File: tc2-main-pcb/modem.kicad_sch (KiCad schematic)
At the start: 15 parts, among them J7 Screw_Terminal_01x01, J8 Conn_01x03, U12 SIM7600G-H-M.2

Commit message: P2 milestone
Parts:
- removed C37: 220nF, Capacitor_SMD:C_0402_1005Metric, symbol Device:C_Small
- removed Card1: SIM-Nano, cacophony-library:SIM-SMD_SMN-304, symbol cacophony-library:SIM-Nano
- removed D4: SMF05CT1G, cacophony-library:SOT-363_L2.0-W1.3-P0.65-LS2.1-BR, symbol cacophony-library:SMF05CT1G
- removed J8: Conn_01x03, Connector_PinHeader_2.54mm:PinHeader_1x03_P2.54mm_Vertical, symbol Connector_Generic:Conn_01x03
- added J11: Conn_01x08, cacophony-library:sim-usb-pcb, symbol Connector_Generic:Conn_01x08
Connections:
- net 4G_USB_D+: now also J11.7 (Pin_7)
- net 4G_USB_D-: now also J11.8 (Pin_8)
- net GND: now also J11.3 (Pin_3), J11.6 (Pin_6)
- net USIM_CLK: now reaches R26.2
- net USIM_CLK: now also J11.2 (Pin_2)
- net USIM_VDD: now reaches U12.36 (USIM_VDD)
- net USIM_VDD: now also J11.5 (Pin_5)
- net USIM_RST: now reaches R25.2
- net USIM_RST: now also J11.1 (Pin_1)
- net USIM_DATA: now reaches R27.2
- net USIM_DATA: now also J11.4 (Pin_4)
- no-connect marks 48 -> 46
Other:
- moved on the sheet: R25, R26, R27

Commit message: P3-Nov release
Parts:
- removed C32, C36: 10uF, Capacitor_SMD:C_0603_1608Metric, symbol Device:C_Small
- added C1 (x4): 220nF, Capacitor_SMD:C_0402_1005Metric, symbol Device:C_Small
- added C4 (x3): 12pF, Capacitor_SMD:C_0402_1005Metric, symbol Device:C_Small
- added C49, C52, C53, C54, C55, C57, C58, C59, C60: 22uF, Capacitor_SMD:C_0603_1608Metric, symbol Device:C_Small
- added FB1: FerriteBead, Inductor_SMD:L_0805_2012Metric, symbol Device:FerriteBead
- added L3: INDUCTOR, Inductor_SMD:L_1008_2520Metric, symbol cacophony-library:Power_Inductor
- added R42, R43: 1M, Resistor_SMD:R_0402_1005Metric, symbol Device:R
- added R44: 100k, Resistor_SMD:R_0402_1005Metric, symbol Device:R
- added R45: 150k, Resistor_SMD:R_0402_1005Metric, symbol Device:R
- added TP3: TP_2P, cacophony-library:test-point-2p, symbol cacophony-library:TestPoint_2Pole
- added U5: TPS6302x, cacophony-library:VSON-14_L4.0-W3.0-P0.50-BL-EP_TI_DSJ, symbol cacophony-library:TPS6302x
- C33, C34, C35: value 10uF -> 22uF; LCSC C19702 -> C2980159
- J7: footprint cacophony-library:SMD_BD4.4-L4.4-D2.8 -> cacophony-library:M2_modem_mount_screw; LCSC C2928178 -> C2928176
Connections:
- net +3V3: no longer C33.1, C34.1, C35.1, U12.2 (VBAT), U12.4 (VBAT), U12.70 (VBAT), U12.72 (VBAT), U12.74 (VBAT)
- net GND: now also C1.1, C1.1, C1.1, C1.1, C4.1, C4.1, C4.1, C49.2, C52.2, C53.2, C54.2, C55.2, C57.2, C58.2, C59.2, C60.2, R44.2, R45.2, TP3.1, U5.15 (PGND), U5.2 (GND)
- new net: R43.2, U5.14 (PG)
- new net: R42.2, R45.1, U5.3 (FB)
- new net +3V8: C1.2, C1.2, C33.1, C34.1, C35.1, C4.2, C4.2, C57.1, C58.1, C59.1, FB1.2, TP3.2, U12.2 (VBAT), U12.4 (VBAT), U12.70 (VBAT), U12.72 (VBAT), U12.74 (VBAT)
- new net +5V: C1.2, C4.2, C54.1, C55.1, U5.10 (VIN), U5.11 (VIN)
- new net 3V3_L1: L3.1, U5.8 (L1), U5.9 (L1)
- new net 3V3_L2: L3.2, U5.6 (L2), U5.7 (L2)
- new net MODEM_3V8: C1.2, C49.1, C52.1, C53.1, C60.1, FB1.1, R42.1, R43.1, U5.4 (VOUT), U5.5 (VOUT)
- new net MODEM_POWER_EN: R44.1, U5.12 (EN)
- no-connect marks 46 -> 48
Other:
- note added: "M2 module mounting screw"
- note added: "SIM7600X-M2_Hardware Design_V1.03.pdf"
- moved on the sheet: J11, J7, R24, R25, R26, R27

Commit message: v0.4.0
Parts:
- C33, C34, C35, C49, C52, C53, C54, C55, C57, C58, C59, C60: LCSC C2980159 -> C86295
- FB1: LCSC C307778 -> C76818
- TP1: renamed from TP3; now left out of the parts list
- renumbered C4 to C32, C1 to C36, C4 to C40, C1 to C45, C4 to C46, C1 to C47, C1 to C51

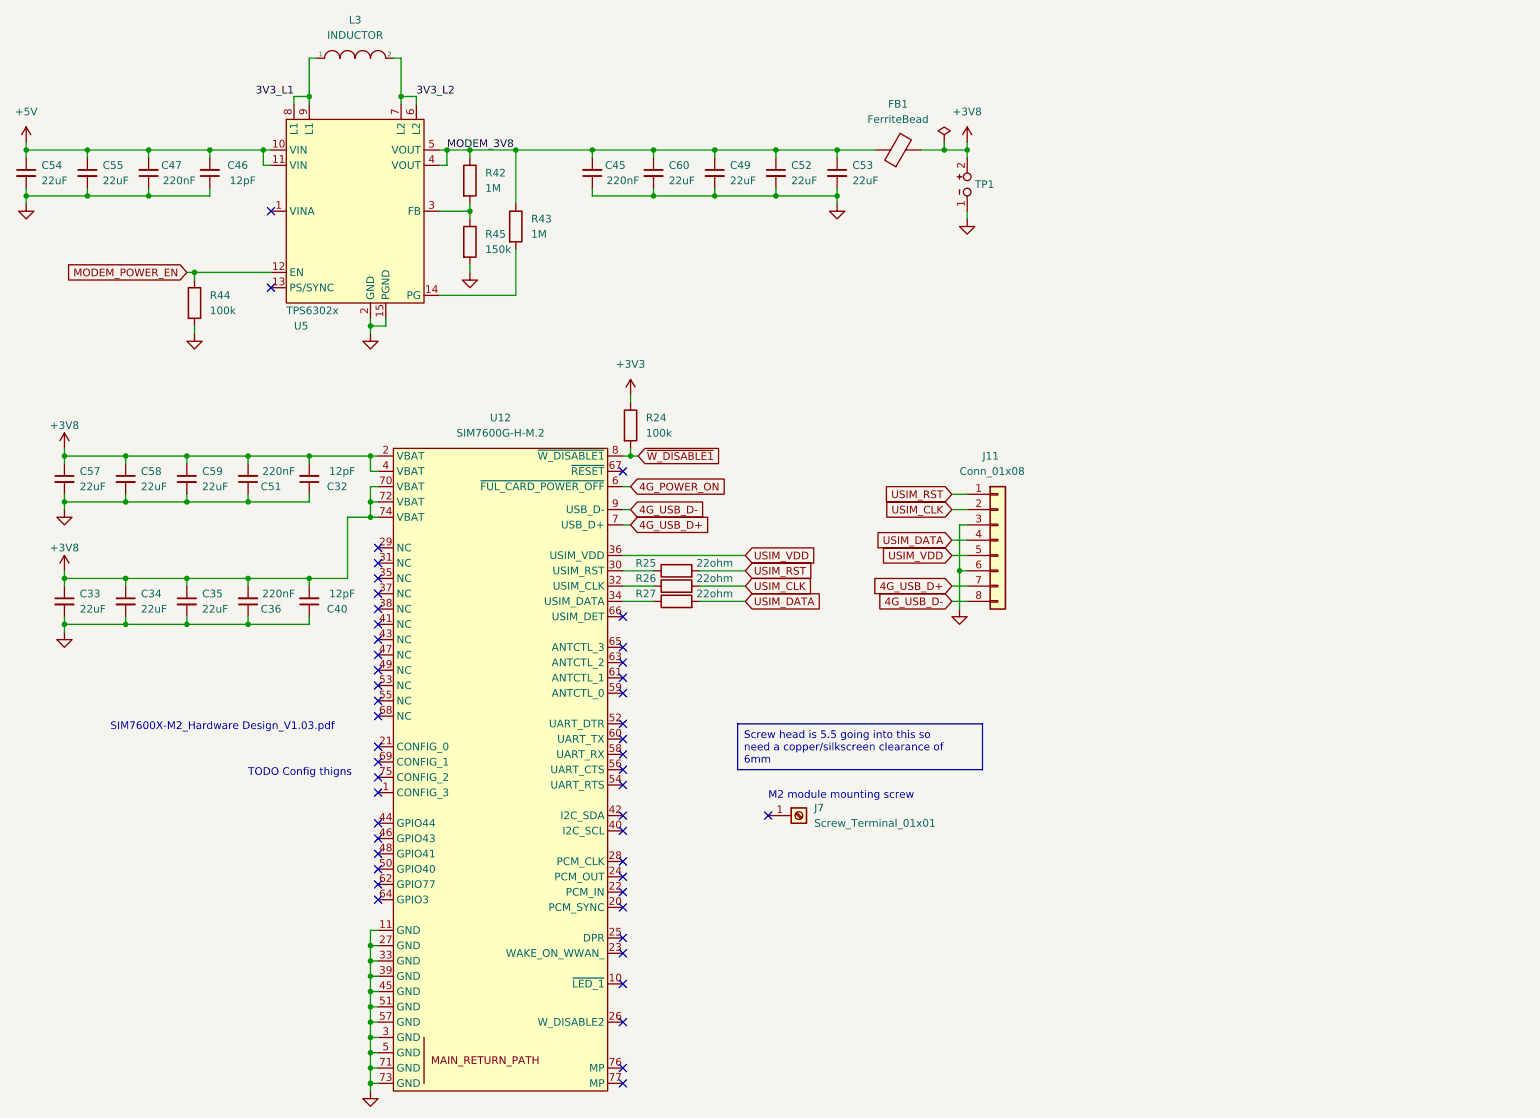
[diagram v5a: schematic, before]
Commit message: Update to use touch sensor
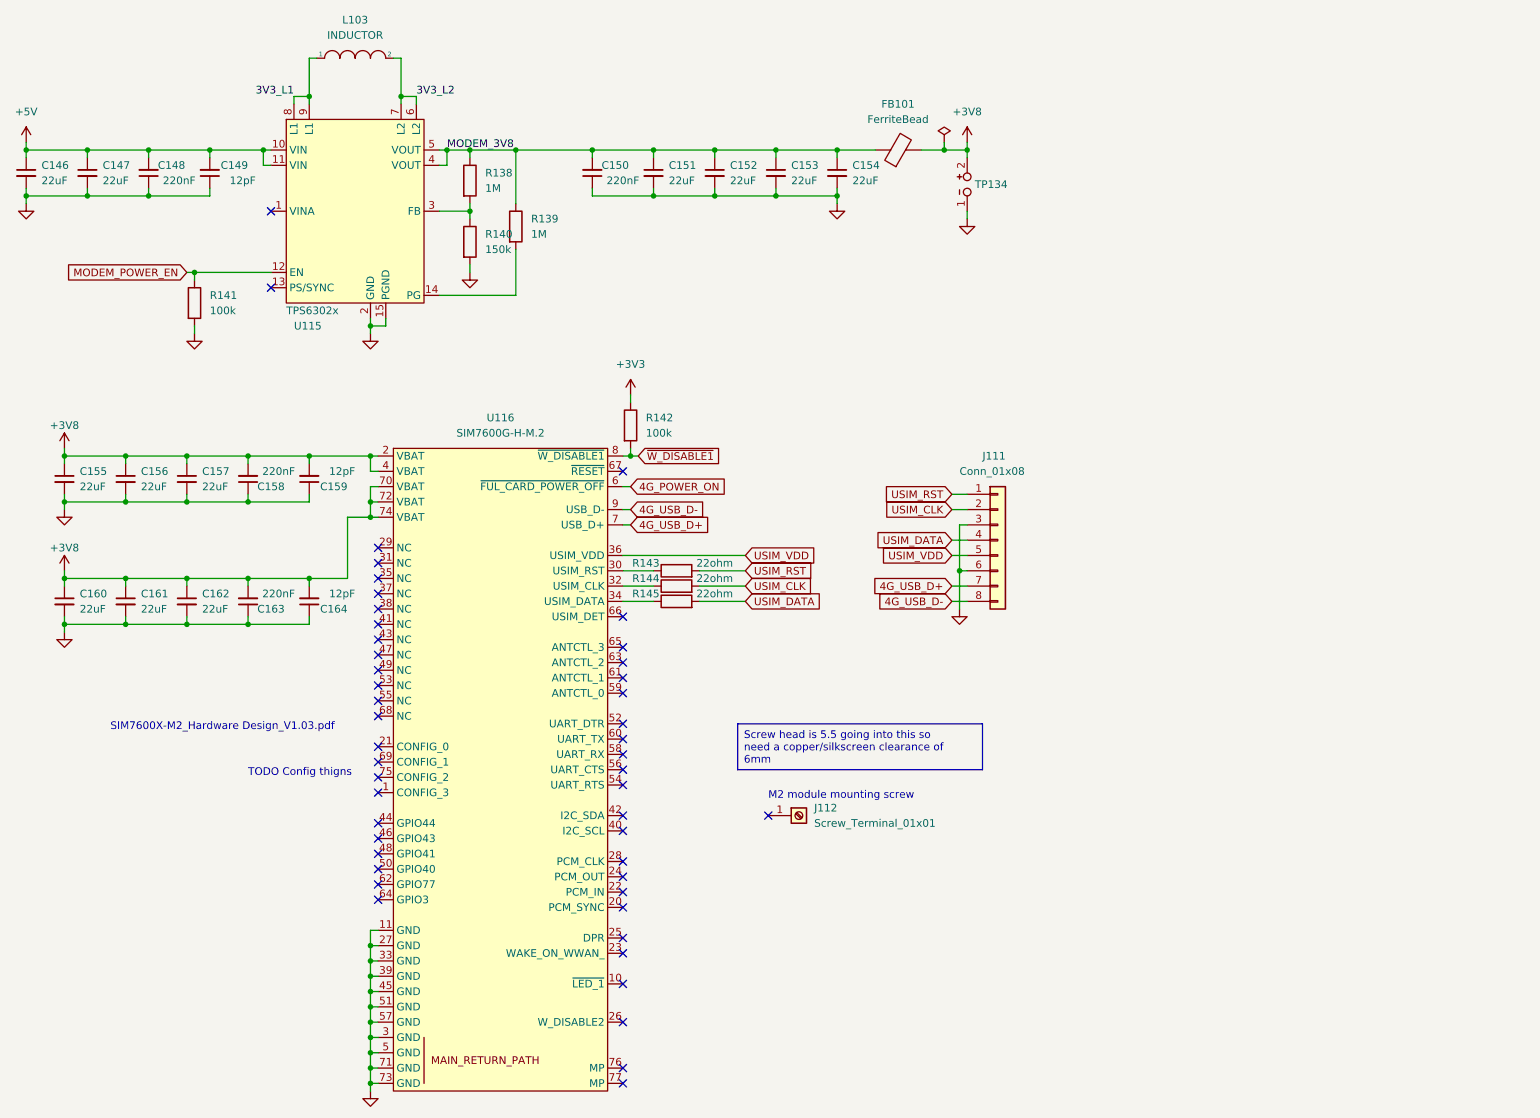
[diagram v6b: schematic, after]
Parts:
- renumbered C54 to C146, C55 to C147, C47 to C148, C46 to C149, C45 to C150, C60 to C151, C49 to C152, C52 to C153, C53 to C154, C57 to C155, C58 to C156, C59 to C157, C51 to C158, C32 to C159, C33 to C160, C34 to C161, C35 to C162, C36 to C163, C40 to C164, FB1 to FB101, J11 to J111, J7 to J112, L3 to L103, R42 to R138, R43 to R139, R45 to R140, R44 to R141, R24 to R142, R25 to R143, R26 to R144, R27 to R145, TP1 to TP134, U5 to U115, U12 to U116

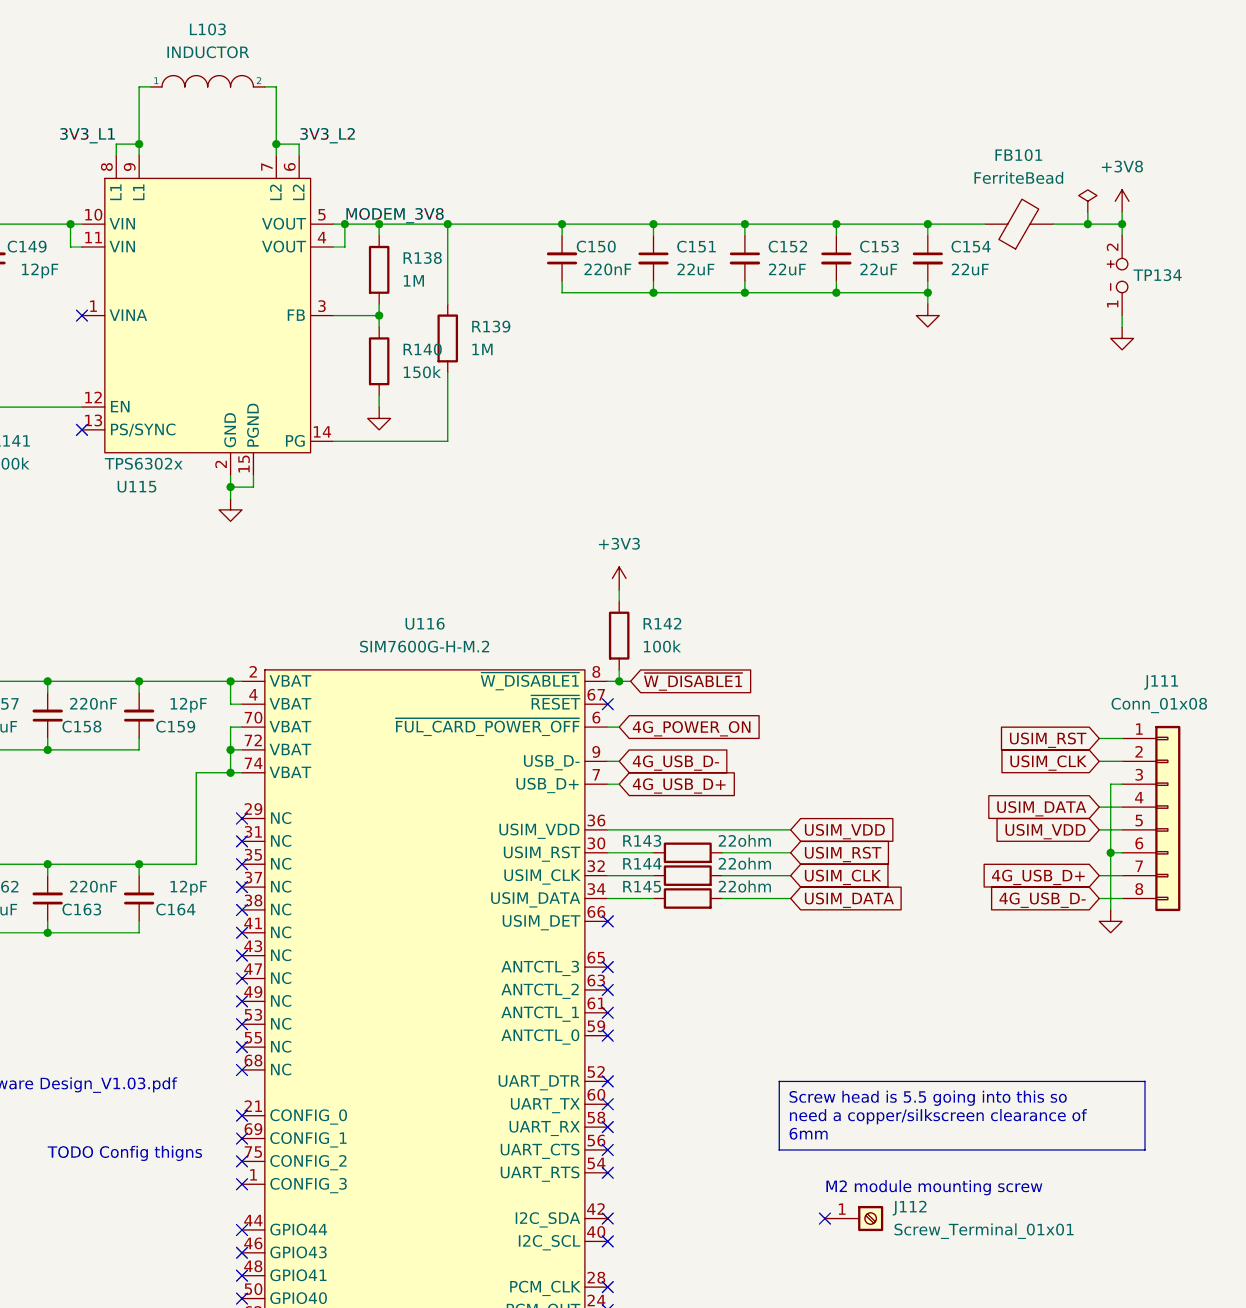
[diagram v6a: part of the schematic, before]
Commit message: Upgraded to new kicad version
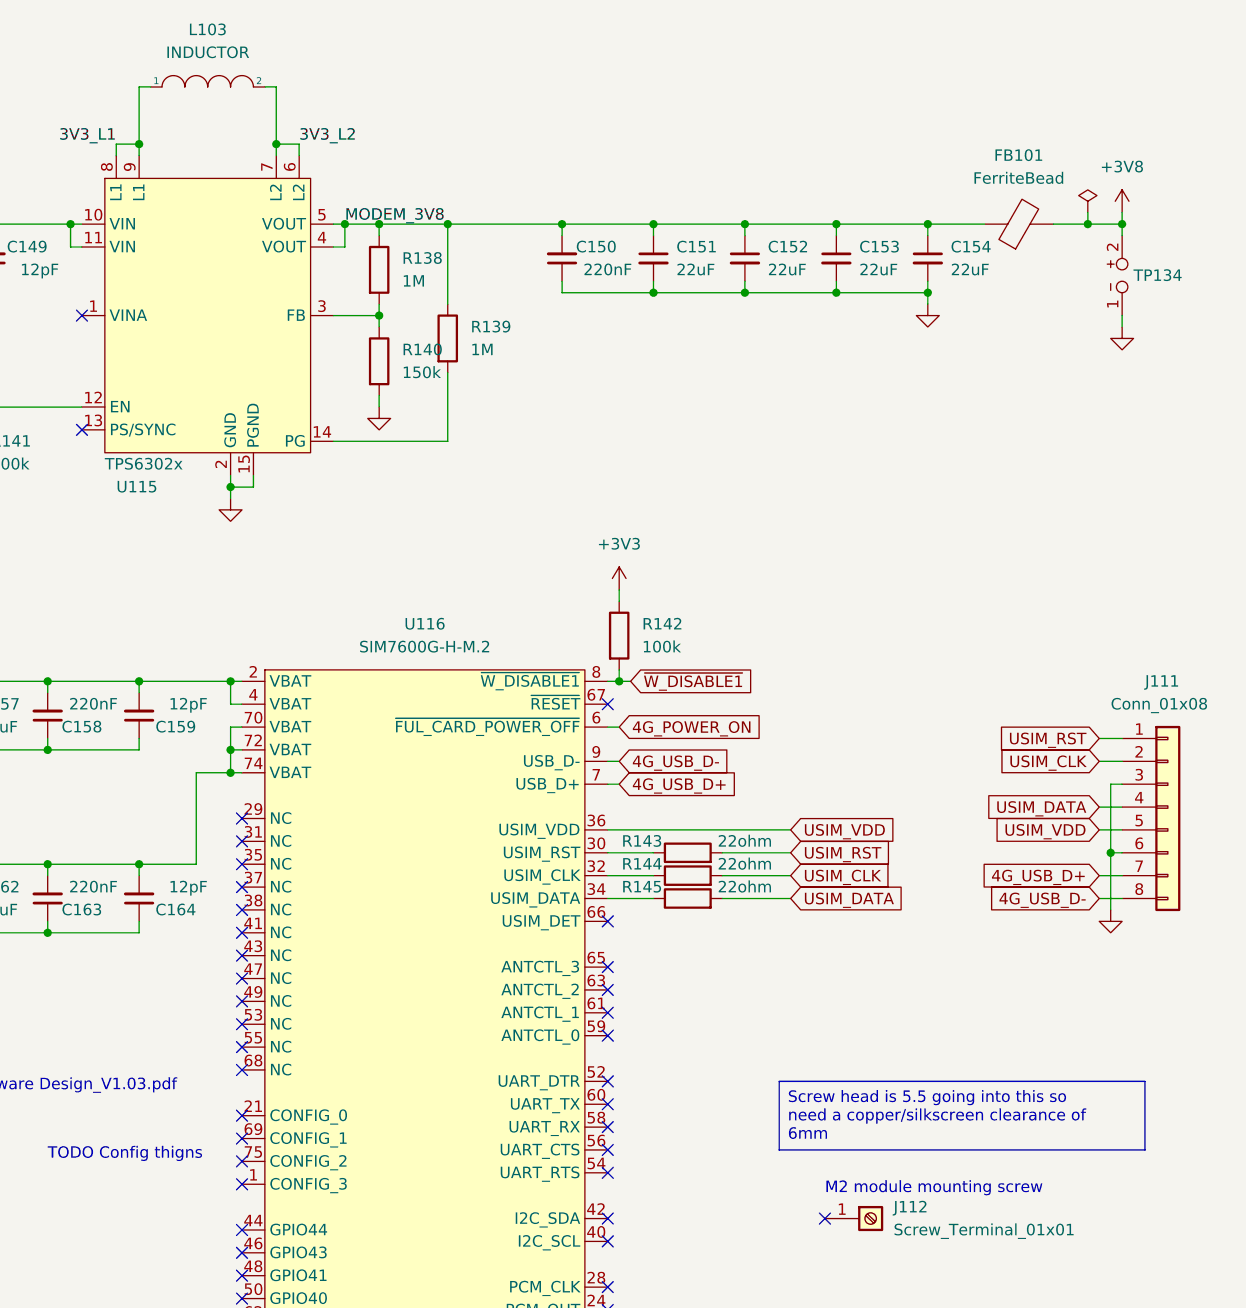
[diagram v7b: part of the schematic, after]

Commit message: Tidy up for making an order for v0.7.3
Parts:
- C146, C147, C151, C152, C153, C154, C155, C156, C157, C160, C161, C162: LCSC C86295 -> (none); LCSC Part (none) -> C86295
- C148, C150, C158, C163: LCSC C16772 -> (none); LCSC Part (none) -> C16772
- C149, C159, C164: LCSC C1547 -> (none); LCSC Part (none) -> C1547
- FB101: LCSC C76818 -> (none); LCSC Part (none) -> C76818
- J112: LCSC C2928176 -> (none); LCSC Part (none) -> C2928176
- L103: LCSC C285917 -> (none); LCSC Part (none) -> C285917
- R138, R139: LCSC C26083 -> (none); LCSC Part (none) -> C26083
- R140: LCSC C25755 -> (none); LCSC Part (none) -> C25755
- R141, R142: LCSC C25741 -> (none); LCSC Part (none) -> C25741
- R143, R144, R145: value 22ohm -> 22Ω; LCSC C25092 -> (none); LCSC Part (none) -> C25092
- U115: LCSC C15483 -> (none); LCSC Part (none) -> C15483
- U116: LCSC C2761526 -> (none); LCSC Part (none) -> C2761526
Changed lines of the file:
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@@
 			)
 		)
-		(property "LCSC" "C16772"
+		(property "LCSC Part" "C16772"
 			(at 71.12 92.71 0)
 			(effects
@@
 			)
 		)
-		(property "Value" "22ohm"
+		(property "Value" "22Ω"
 			(at 148.59 109.22 90)
 			(effects
@@
 			)
 		)
-		(property "LCSC" "C25092"
+		(property "LCSC Part" "C25092"
 			(at 142.24 110.49 0)
 			(effects
@@
 			)
 		)
-		(property "LCSC" "C285917"
+		(property "LCSC Part" "C285917"
 			(at 88.9 22.86 0)
 			(effects
@@
 			)
 		)
-		(property "LCSC" "C1547"
+		(property "LCSC Part" "C1547"
 			(at 81.28 92.71 0)
 			(effects
@@
 			)
 		)
-		(property "LCSC" "C86295"
+		(property "LCSC Part" "C86295"
 			(at 34.29 41.91 0)
 			(effects
@@
 			)
 		)
-		(property "LCSC" "C86295"
+		(property "LCSC Part" "C86295"
 			(at 40.64 92.71 0)
 			(effects
@@
 			)
 		)
-		(property "LCSC" "C1547"
+		(property "LCSC Part" "C1547"
 			(at 64.77 41.91 0)
 			(effects
@@
 			)
 		)
-		(property "LCSC" "C86295"
+		(property "LCSC Part" "C86295"
 			(at 168.91 41.91 0)
 			(effects
@@
 			)
 		)
-		(property "LCSC" "C16772"
+		(property "LCSC Part" "C16772"
 			(at 71.12 113.03 0)
 			(effects
@@
 			)
 		)
-		(property "LCSC" "C26083"
+		(property "LCSC Part" "C26083"
 			(at 115.57 50.8 0)
 			(effects
@@
 			)
 		)
-		(property "LCSC" "C16772"
+		(property "LCSC Part" "C16772"
 			(at 128.27 41.91 0)
 			(effects
@@
 			)
 		)
-		(property "LCSC" "C86295"
+		(property "LCSC Part" "C86295"
 			(at 50.8 92.71 0)
 			(effects
@@
 			)
 		)
-		(property "LCSC" "C86295"
+		(property "LCSC Part" "C86295"
 			(at 60.96 113.03 0)
 			(effects
@@
 			)
 		)
-		(property "LCSC" "C86295"
+		(property "LCSC Part" "C86295"
 			(at 60.96 92.71 0)
 			(effects
@@
 			)
 		)
-		(property "Value" "22ohm"
+		(property "Value" "22Ω"
 			(at 148.59 111.76 90)
 			(effects
@@
 			)
 		)
-		(property "LCSC" "C25092"
+		(property "LCSC Part" "C25092"
 			(at 142.24 113.03 0)
 			(effects
@@
 			)
 		)
-		(property "LCSC" "C86295"
+		(property "LCSC Part" "C86295"
 			(at 158.75 41.91 0)
 			(effects
@@
 			)
 		)
-		(property "Value" "22ohm"
+		(property "Value" "22Ω"
 			(at 148.59 106.68 90)
 			(effects
@@
 			)
 		)
-		(property "LCSC" "C25092"
+		(property "LCSC Part" "C25092"
 			(at 142.24 107.95 0)
 			(effects
@@
 			)
 		)
-		(property "LCSC" "C86295"
+		(property "LCSC Part" "C86295"
 			(at 40.64 113.03 0)
 			(effects
@@
 			)
 		)
-		(property "LCSC" "C76818"
+		(property "LCSC Part" "C76818"
 			(at 179.07 38.1 0)
 			(effects
@@
 			)
 		)
-		(property "LCSC" "C25755"
+		(property "LCSC Part" "C25755"
 			(at 107.95 53.34 0)
 			(effects
@@
 			)
 		)
-		(property "LCSC" "C25741"
+		(property "LCSC Part" "C25741"
 			(at 62.23 63.5 0)
 			(effects
@@
 			)
 		)
-		(property "LCSC" "C25741"
+		(property "LCSC Part" "C25741"
 			(at 134.62 83.82 0)
 			(effects
@@
 			)
 		)
-		(property "LCSC" "C86295"
+		(property "LCSC Part" "C86295"
 			(at 44.45 41.91 0)
 			(effects
@@
 			)
 		)
-		(property "LCSC" "C86295"
+		(property "LCSC Part" "C86295"
 			(at 50.8 113.03 0)
 			(effects
@@
 			)
 		)
-		(property "LCSC" "C2928176"
+		(property "LCSC Part" "C2928176"
 			(at 162.56 148.59 0)
 			(effects
@@
 			)
 		)
-		(property "LCSC" "C16772"
+		(property "LCSC Part" "C16772"
 			(at 54.61 41.91 0)
 			(effects
@@
 			)
 		)
-		(property "LCSC" "C1547"
+		(property "LCSC Part" "C1547"
 			(at 81.28 113.03 0)
 			(effects
@@
 			)
 		)
-		(property "LCSC" "C86295"
+		(property "LCSC Part" "C86295"
 			(at 148.59 41.91 0)
 			(effects
@@
 			)
 		)
-		(property "LCSC" "C15483"
+		(property "LCSC Part" "C15483"
 			(at 85.09 25.4 0)
 			(effects
@@
 			)
 		)
-		(property "LCSC" "C86295"
+		(property "LCSC Part" "C86295"
 			(at 138.43 41.91 0)
 			(effects
@@
 			)
 		)
-		(property "LCSC" "C2761526"
+		(property "LCSC Part" "C2761526"
 			(at 107.95 86.36 0)
 			(effects
@@
 			)
 		)
-		(property "LCSC" "C26083"
+		(property "LCSC Part" "C26083"
 			(at 107.95 43.18 0)
 			(effects
